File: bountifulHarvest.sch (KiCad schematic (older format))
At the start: 0 parts

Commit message: added endstops
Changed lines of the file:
@@
 4 Encoders\n7Pin connectors\n
 Wire Notes Line
-	7600 1550 7600 2100
-Wire Notes Line
-	7600 2100 6050 2100
-Wire Notes Line
-	6050 2100 6050 1550
-Wire Notes Line
-	6050 1550 7600 1550
-Text Notes 6450 1900 0    50   ~ 0
+	7600 550  7600 1100
+Wire Notes Line
+	7600 1100 6050 1100
+Wire Notes Line
+	6050 1100 6050 550
+Wire Notes Line
+	6050 550  7600 550
+Text Notes 6450 900  0    50   ~ 0
 Main Processor\nArduino atmega2570
 Wire Notes Line
@@
 Wire Notes Line
 	5650 5900 5650 6300
-$Sheet
-S 6050 2300 1650 3000
-U 5EE66603
-F0 "Main Processor" 100
-F1 "ATMEGA2560.sch" 100
-F2 "SCK_SPI" I R 7700 2800 79
-F3 "SDI_SPI" I R 7700 2950 79
-F4 "SDO_SPI" I R 7700 3100 79
-F5 "X_[0..4]" I R 7700 3450 79
-F6 "Y_[0..4]" I R 7700 3600 79
-F7 "Z_[0..4]" I R 7700 3800 79
-F8 "X2_[0..4]" I R 7700 3300 79
-F9 "P_0_I" I L 6050 5000 59
-F10 "P_1_I" I L 6050 4850 59
-F11 "P_2_I" I L 6050 4700 59
-F12 "P_3_I" I L 6050 4550 59
-F13 "periph_0" I R 7700 5000 59
-F14 "periph_1" I R 7700 4850 59
-F15 "periph_2" I R 7700 4700 59
-F16 "periph_3" I R 7700 4550 59
-F17 "~CS_cop" O L 6050 2700 59
-F18 "TX" I L 6050 2900 59
-F19 "RX" I L 6050 2800 59
-F20 "~CS~_SPI" I L 6050 2500 59
-F21 "CO_P_RESET" I L 6050 3200 59
-$EndSheet
 Wire Wire Line
 	10100 950  9250 950
@@
 	7700 3300 9550 3300
 Wire Wire Line
-	6050 5000 4150 5000
-Wire Wire Line
-	4150 5000 4150 6650
+	6050 5200 4150 5200
+Wire Wire Line
+	4150 5200 4150 6650
 Wire Wire Line
 	4150 6650 4350 6650
@@
 	4350 6750 4000 6750
 Wire Wire Line
-	4000 6750 4000 4850
-Wire Wire Line
-	4000 4850 6050 4850
-Wire Wire Line
-	6050 4700 3900 4700
-Wire Wire Line
-	3900 4700 3900 6850
+	4000 6750 4000 5050
+Wire Wire Line
+	4000 5050 6050 5050
+Wire Wire Line
+	6050 4900 3900 4900
+Wire Wire Line
+	3900 4900 3900 6850
 Wire Wire Line
 	3900 6850 4350 6850
 Wire Wire Line
-	6050 4550 3850 4550
-Wire Wire Line
-	3850 4550 3850 6950
+	6050 4750 3850 4750
+Wire Wire Line
+	3850 4750 3850 6950
 Wire Wire Line
 	3850 6950 4350 6950
@@
 Wire Wire Line
 	3100 3650 2050 3650
+$Sheet
+S 6050 2300 1650 3000
+U 5EE66603
+F0 "Main Processor" 100
+F1 "ATMEGA2560.sch" 100
+F2 "SCK_SPI" I R 7700 2800 79
+F3 "SDI_SPI" I R 7700 2950 79
+F4 "SDO_SPI" I R 7700 3100 79
+F5 "X_[0..4]" I R 7700 3450 79
+F6 "Y_[0..4]" I R 7700 3600 79
+F7 "Z_[0..4]" I R 7700 3800 79
+F8 "X2_[0..4]" I R 7700 3300 79
+F9 "P_0_I" I L 6050 5200 59
+F10 "P_1_I" I L 6050 5050 59
+F11 "P_2_I" I L 6050 4900 59
+F12 "P_3_I" I L 6050 4750 59
+F13 "periph_0" I R 7700 5000 59
+F14 "periph_1" I R 7700 4850 59
+F15 "periph_2" I R 7700 4700 59
+F16 "periph_3" I R 7700 4550 59
+F17 "~CS_cop" O L 6050 2700 59
+F18 "TX" I L 6050 2900 59
+F19 "RX" I L 6050 2800 59
+F20 "~CS~_SPI" I L 6050 2500 59
+F21 "CO_P_RESET" I L 6050 3200 59
+$EndSheet
 $EndSCHEMATC

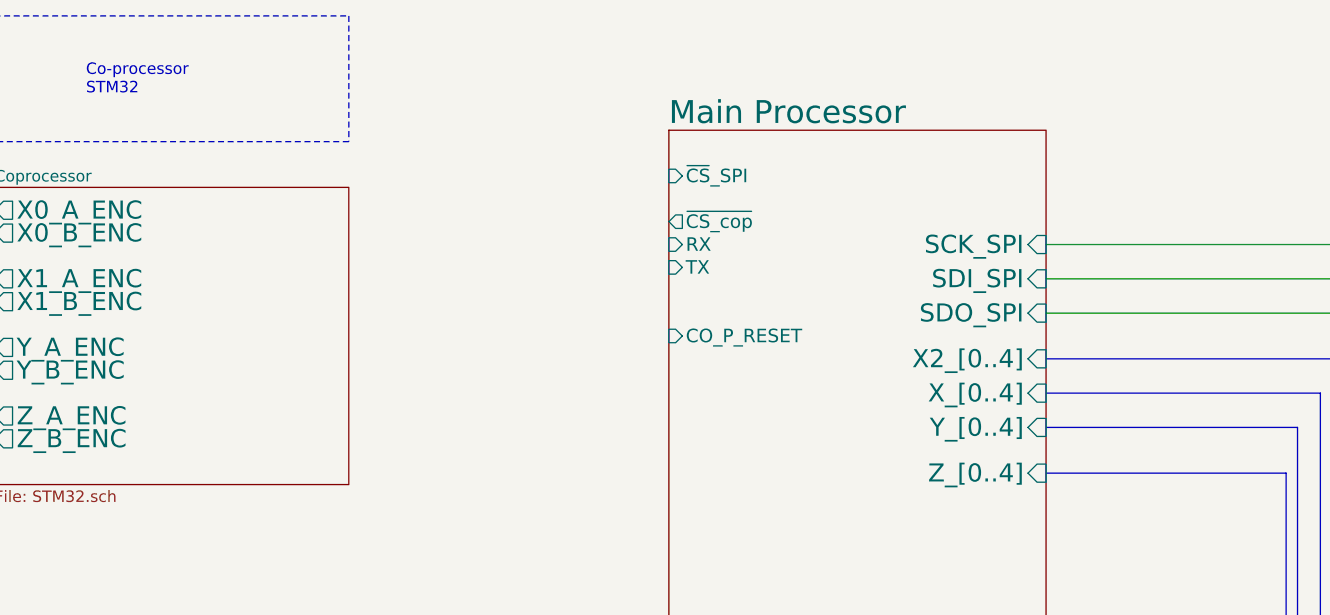
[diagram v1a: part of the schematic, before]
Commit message: connected CoP + mP SPI. pushed updated into layout
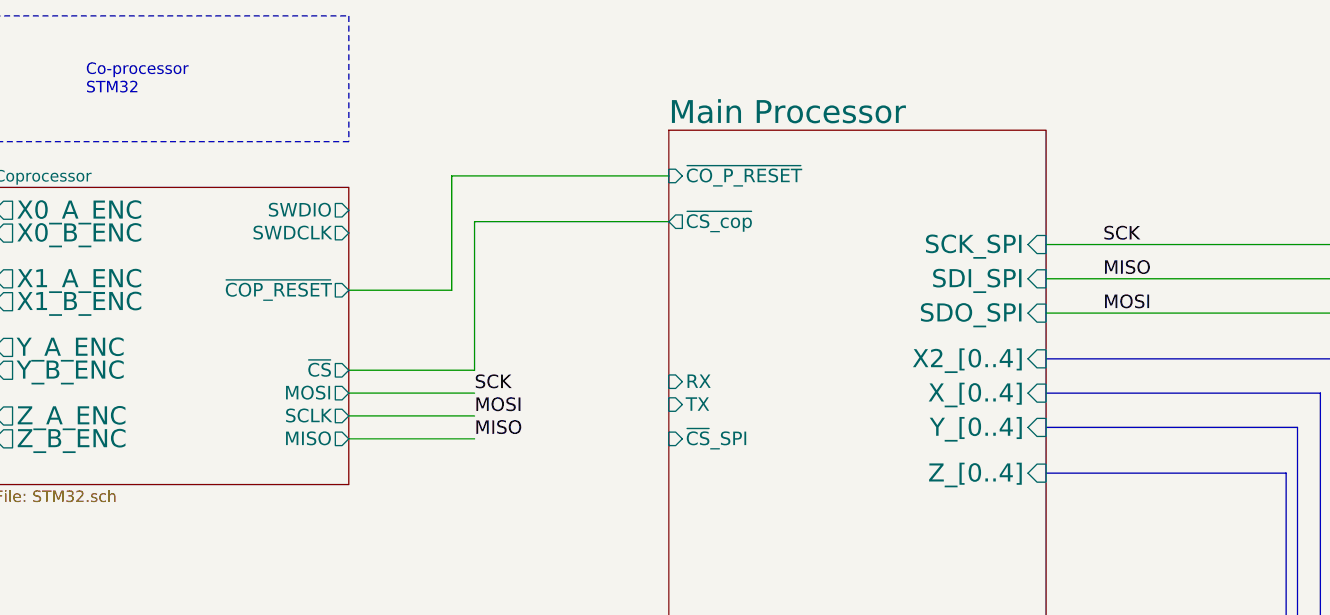
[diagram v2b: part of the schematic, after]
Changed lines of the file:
@@
 F8 "Z_A_ENC" O L 3100 3550 79
 F9 "Z_B_ENC" O L 3100 3650 79
+F10 "SWDIO" O R 4650 2650 59
+F11 "SWDCLK" O R 4650 2750 59
+F12 "~COP_RESET" O R 4650 3000 59
+F13 "~CS" O R 4650 3350 59
+F14 "MOSI" O R 4650 3450 59
+F15 "SCLK" O R 4650 3550 59
+F16 "MISO" O R 4650 3650 59
 $EndSheet
 Wire Notes Line
@@
 F16 "periph_3" I R 7700 4550 59
 F17 "~CS_cop" O L 6050 2700 59
-F18 "TX" I L 6050 2900 59
-F19 "RX" I L 6050 2800 59
-F20 "~CS~_SPI" I L 6050 2500 59
-F21 "CO_P_RESET" I L 6050 3200 59
-$EndSheet
+F18 "TX" I L 6050 3500 59
+F19 "RX" I L 6050 3400 59
+F20 "~CS~_SPI" I L 6050 3650 59
+F21 "~CO_P_RESET" I L 6050 2500 59
+$EndSheet
+Wire Wire Line
+	5100 2500 5100 3000
+Wire Wire Line
+	5100 3000 4650 3000
+Wire Wire Line
+	5100 2500 6050 2500
+Wire Wire Line
+	6050 2700 5200 2700
+Wire Wire Line
+	5200 2700 5200 3350
+Wire Wire Line
+	5200 3350 4650 3350
+Text Label 5200 3450 0    59   ~ 0
+SCK
+Text Label 5200 3550 0    59   ~ 0
+MOSI
+Text Label 5200 3650 0    59   ~ 0
+MISO
+Text Label 7950 2800 0    59   ~ 0
+SCK
+Text Label 7950 3100 0    59   ~ 0
+MOSI
+Text Label 7950 2950 0    59   ~ 0
+MISO
+Wire Wire Line
+	5200 3450 4650 3450
+Wire Wire Line
+	4650 3550 5200 3550
+Wire Wire Line
+	5200 3650 4650 3650
 $EndSCHEMATC

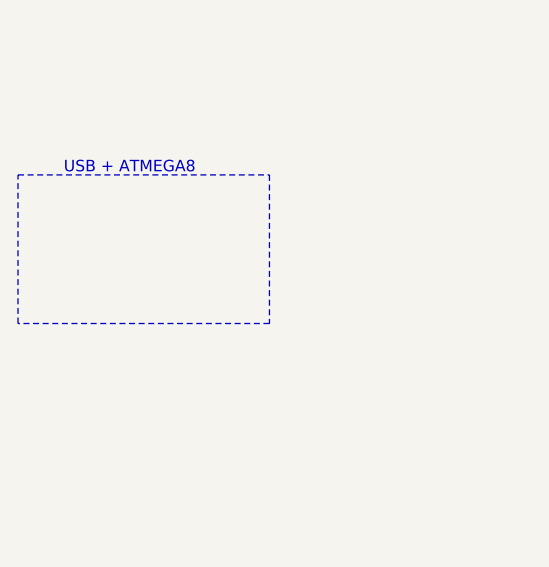
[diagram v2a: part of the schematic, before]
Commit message: added  atmega16. finished CoP. need check VBUS <-> ATMEGA supplies
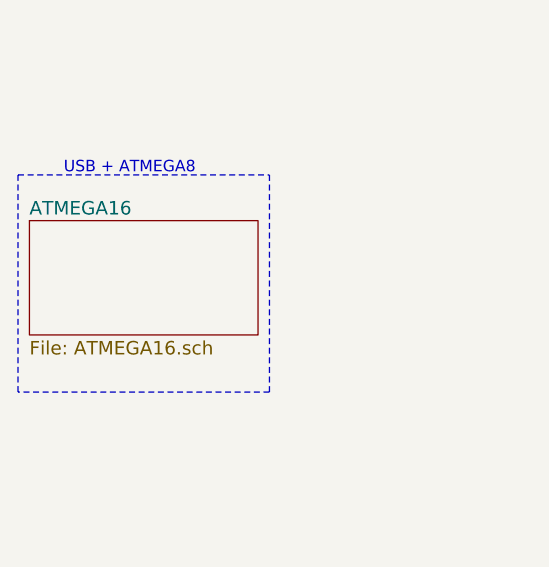
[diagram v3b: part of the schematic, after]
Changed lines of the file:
@@
 $Descr A4 11693 8268
 encoding utf-8
-Sheet 1 8
+Sheet 1 9
 Title "BountifulHarvest"
 Date ""
@@
 	1000 4850 2100 4850
 Wire Notes Line
-	2100 4850 2100 5500
-Wire Notes Line
-	2100 5500 1000 5500
-Wire Notes Line
-	1000 5500 1000 4850
+	2100 4850 2100 5800
+Wire Notes Line
+	2100 5800 1000 5800
+Wire Notes Line
+	1000 5800 1000 4850
 Text Notes 1200 4850 0    50   ~ 0
 USB + ATMEGA8
@@
 Wire Wire Line
 	5200 3650 4650 3650
+$Sheet
+S 1050 5050 1000 500
+U 6318D4AB
+F0 "ATMEGA16" 59
+F1 "ATMEGA16.sch" 59
+$EndSheet
 $EndSCHEMATC
